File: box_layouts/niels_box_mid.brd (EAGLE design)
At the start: 100 x 80 mm, 0 parts

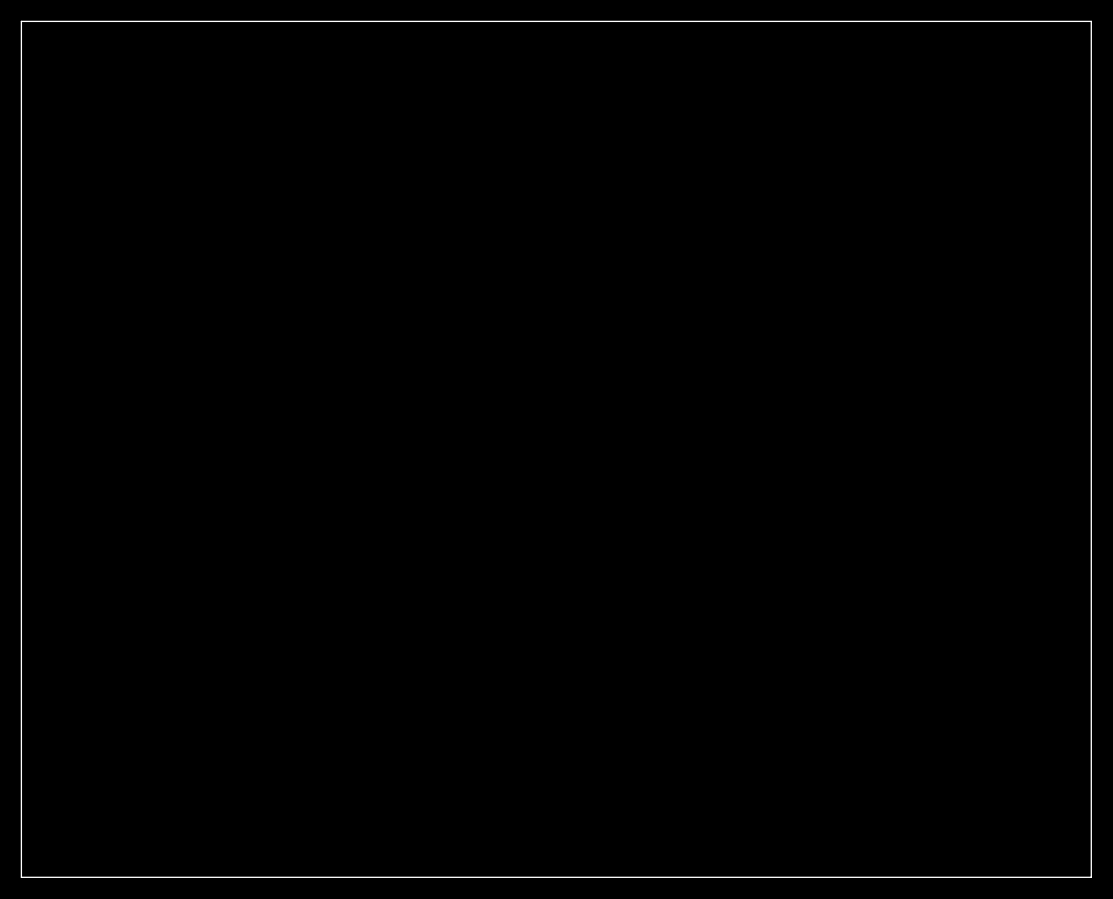
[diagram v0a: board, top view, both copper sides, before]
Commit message: * updated niels box middle board * usb power splicer board started
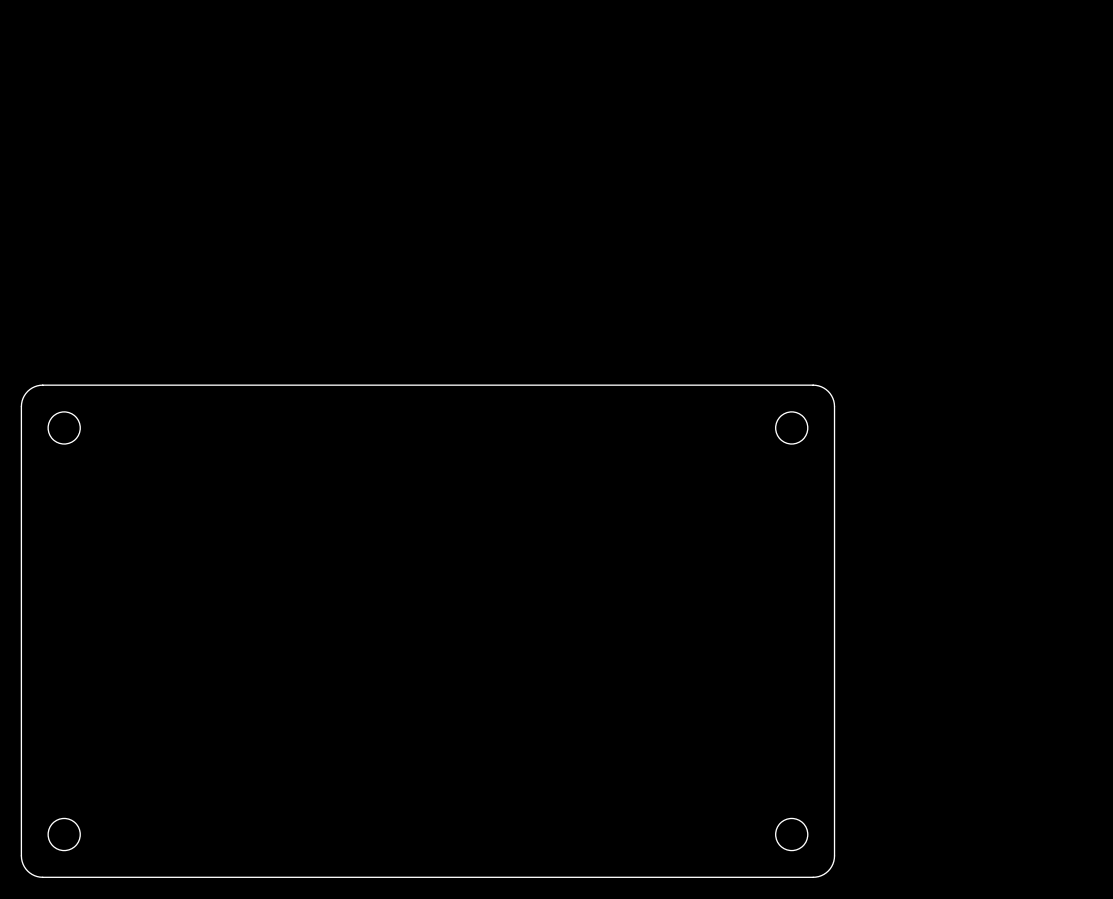
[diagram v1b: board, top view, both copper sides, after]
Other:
- board size 100 x 80 mm -> 76 x 46 mm
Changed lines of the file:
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@@
 <setting verticaltext="up"/>
 </settings>
-<grid distance="0.05" unitdist="inch" unit="inch" style="lines" multiple="1" display="no" altdistance="0.025" altunitdist="inch" altunit="inch"/>
+<grid distance="1" unitdist="mm" unit="mm" style="lines" multiple="1" display="yes" altdistance="0.025" altunitdist="inch" altunit="inch"/>
 <layers>
 <layer number="1" name="Top" color="4" fill="1" visible="yes" active="yes"/>
@@
 <layer number="43" name="vRestrict" color="2" fill="10" visible="yes" active="yes"/>
 <layer number="44" name="Drills" color="7" fill="1" visible="no" active="yes"/>
-<layer number="45" name="Holes" color="7" fill="1" visible="no" active="yes"/>
+<layer number="45" name="Holes" color="7" fill="1" visible="yes" active="yes"/>
 <layer number="46" name="Milling" color="3" fill="1" visible="no" active="yes"/>
 <layer number="47" name="Measures" color="7" fill="1" visible="no" active="yes"/>
@@
 <board>
 <plain>
-<wire x1="0" y1="0" x2="100" y2="0" width="0" layer="20"/>
-<wire x1="100" y1="0" x2="100" y2="80" width="0" layer="20"/>
-<wire x1="100" y1="80" x2="0" y2="80" width="0" layer="20"/>
-<wire x1="0" y1="80" x2="0" y2="0" width="0" layer="20"/>
+<wire x1="0" y1="44" x2="2" y2="46" width="0" layer="20" curve="-90"/>
+<wire x1="2" y1="46" x2="74" y2="46" width="0" layer="20"/>
+<wire x1="74" y1="46" x2="76" y2="44" width="0" layer="20" curve="-90"/>
+<wire x1="76" y1="44" x2="76" y2="2" width="0" layer="20"/>
+<wire x1="76" y1="2" x2="74" y2="0" width="0" layer="20" curve="-90"/>
+<wire x1="74" y1="0" x2="2" y2="0" width="0" layer="20"/>
+<wire x1="2" y1="0" x2="0" y2="2" width="0" layer="20" curve="-90"/>
+<wire x1="0" y1="2" x2="0" y2="44" width="0" layer="20"/>
+<hole x="4" y="4" drill="3"/>
+<hole x="4" y="42" drill="3"/>
+<hole x="72" y="4" drill="3"/>
+<hole x="72" y="42" drill="3"/>
 </plain>
 <attributes>
